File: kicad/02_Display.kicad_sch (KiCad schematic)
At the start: 0 parts

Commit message: Wire 02_Display: LCD (2-unit), JST-A/JST-B, backlight switch
LCD's power unit (VCC/GND/LED/RESET) wired to JST-A (4-pin), SPI+
touch unit (CS/DC/MOSI/SCK/MISO/T_CS/T_IRQ) wired to JST-B (7-pin),
each JST pin sharing its net with the corresponding LCD symbol pin
per the cable-connected-module pattern used throughout. VCC stays
on 3V3; LED (backlight) switches via a second AO3400A off VBAT_OUT,
gate driven by LCD_BL_GATE through a 100R series resistor with a
10k gate pull-down so the backlight defaults off during boot.

ERC: 0 errors, 18 warnings, all isolated labels for sheets not yet
wired -- exactly the expected set (9 fewer than before, matching
this sheet's 9 LCD_* labels resolving against 01_MCU).

Co-Authored-By: Claude Sonnet 5 <noreply@anthropic.com>
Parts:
- added J4: Conn_01x04, Connector_JST:JST_PH_B4B-PH-K_1x04_P2.00mm_Vertical, symbol Connector_Generic:Conn_01x04
- added J5: Conn_01x07, Connector_JST:JST_PH_B7B-PH-K_1x07_P2.00mm_Vertical, symbol Connector_Generic:Conn_01x07
- added Q1: AO3400A, Package_TO_SOT_SMD:SOT-23, symbol Transistor_FET:AO3400A
- added R13: 100, Package_TO_SOT_SMD:SOT-23, symbol Device:R_Small
- added R14: 10k, symbol Device:R_Small
- added U5: (no value), symbol DeskBuddy:LCD
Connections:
- new net: Q1.1 (G), R13.2, R14.2
- new net +3V3: J4.1 (Pin_1), U5.1 (VCC)
- new net GND: J4.2 (Pin_2), Q1.2 (S), R14.1, U5.2 (GND)
- new net LCD_BL_GATE: R13.1
- new net LCD_CS: J5.1 (Pin_1), U5.5 (CS)
- new net LCD_DC: J5.2 (Pin_2), U5.6 (DC)
- new net LCD_MISO: J5.5 (Pin_5), U5.9 (MISO)
- new net LCD_MOSI: J5.3 (Pin_3), U5.7 (MOSI)
- new net LCD_RESET: J4.4 (Pin_4), U5.4 (RESET)
- new net LCD_SCK: J5.4 (Pin_4), U5.8 (SCK)
- new net LCD_T_CS: J5.6 (Pin_6), U5.10 (T_CS)
- new net LCD_T_IRQ: J5.7 (Pin_7), U5.11 (T_IRQ)
- new net VBAT_OUT: J4.3 (Pin_3), Q1.3 (D), U5.3 (LED)

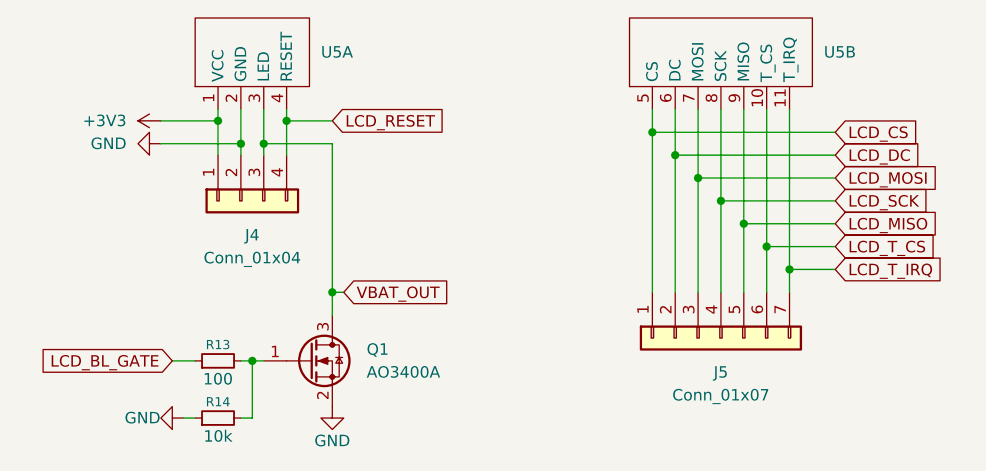
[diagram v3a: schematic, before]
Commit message: Wire 03_Sensors_I2C0: ToF, AHT20+BMP280, MPU6050
Three internal-bus sensors each wired symbol-to-JST on shared nets
(6-pin for ToF incl. INT/SHUT, 4-pin each for AHT20+BMP280 and
MPU6050), all on I2C0_SDA/I2C0_SCL with one pair of 4.7k pull-ups
to 3V3 for the whole bus.

ERC: 0 errors, 14 warnings, all isolated labels for sheets not yet
wired -- 4 fewer than before (I2C0_SDA, I2C0_SCL, TOF_INT, TOF_SHUT
now resolved against 01_MCU).

Co-Authored-By: Claude Sonnet 5 <noreply@anthropic.com>
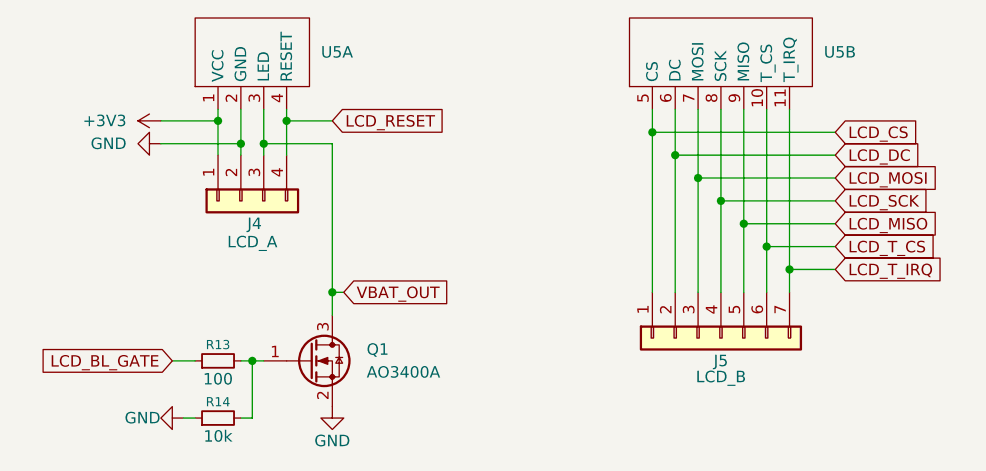
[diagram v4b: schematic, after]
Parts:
- J4: value Conn_01x04 -> LCD_A
- J5: value Conn_01x07 -> LCD_B
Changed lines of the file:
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@@
 		(dnp no)
 		(property "Reference" "J5"
-			(at 96.52 57.15 90)
+			(at 96.52 55.88 90)
 			(show_name no)
 			(do_not_autoplace no)
@@
 			)
 		)
-		(property "Value" "Conn_01x07"
-			(at 96.52 59.69 90)
+		(property "Value" "LCD_B"
+			(at 96.52 57.658 90)
 			(show_name no)
 			(do_not_autoplace no)
@@
 		(dnp no)
 		(property "Reference" "J4"
-			(at 44.45 41.91 90)
+			(at 44.704 40.64 90)
 			(show_name no)
 			(do_not_autoplace no)
@@
 			)
 		)
-		(property "Value" "Conn_01x04"
-			(at 44.45 44.45 90)
+		(property "Value" "LCD_A"
+			(at 44.45 42.672 90)
 			(show_name no)
 			(do_not_autoplace no)

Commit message: Footprint atamaları düzeltildi, satın alım listesi eklendi
- R/C/LED 0805, USB-C USB4110, tactile switch PTS645SM43SMTR92
- C6 47uF 1206, D5 BAT54 yerine SS14 (SMA)
- J8 JST ve TestPoint footprint'leri atandı
- purchase-list.md eklendi, BOM/plan/notlar güncellendi

Co-Authored-By: Claude Sonnet 5.5 <noreply@anthropic.com>
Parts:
- R13: footprint Package_TO_SOT_SMD:SOT-23 -> Resistor_SMD:R_0805_2012Metric
- R14: footprint (none) -> Resistor_SMD:R_0805_2012Metric
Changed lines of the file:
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@@
 			)
 		)
-		(property "Footprint" ""
+		(property "Footprint" "Resistor_SMD:R_0805_2012Metric"
 			(at 40.64 62.23 0)
 			(hide yes)
@@
 			)
 		)
-		(property "Footprint" "Package_TO_SOT_SMD:SOT-23"
+		(property "Footprint" "Resistor_SMD:R_0805_2012Metric"
 			(at 40.64 55.88 0)
 			(hide yes)
